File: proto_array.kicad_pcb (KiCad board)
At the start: 2 copper layers, 99.1 x 129.5 mm, 55 parts, among them P1 CONN_01X03, U1 ADS131E08, U2 BEAGLEBONEBLACK

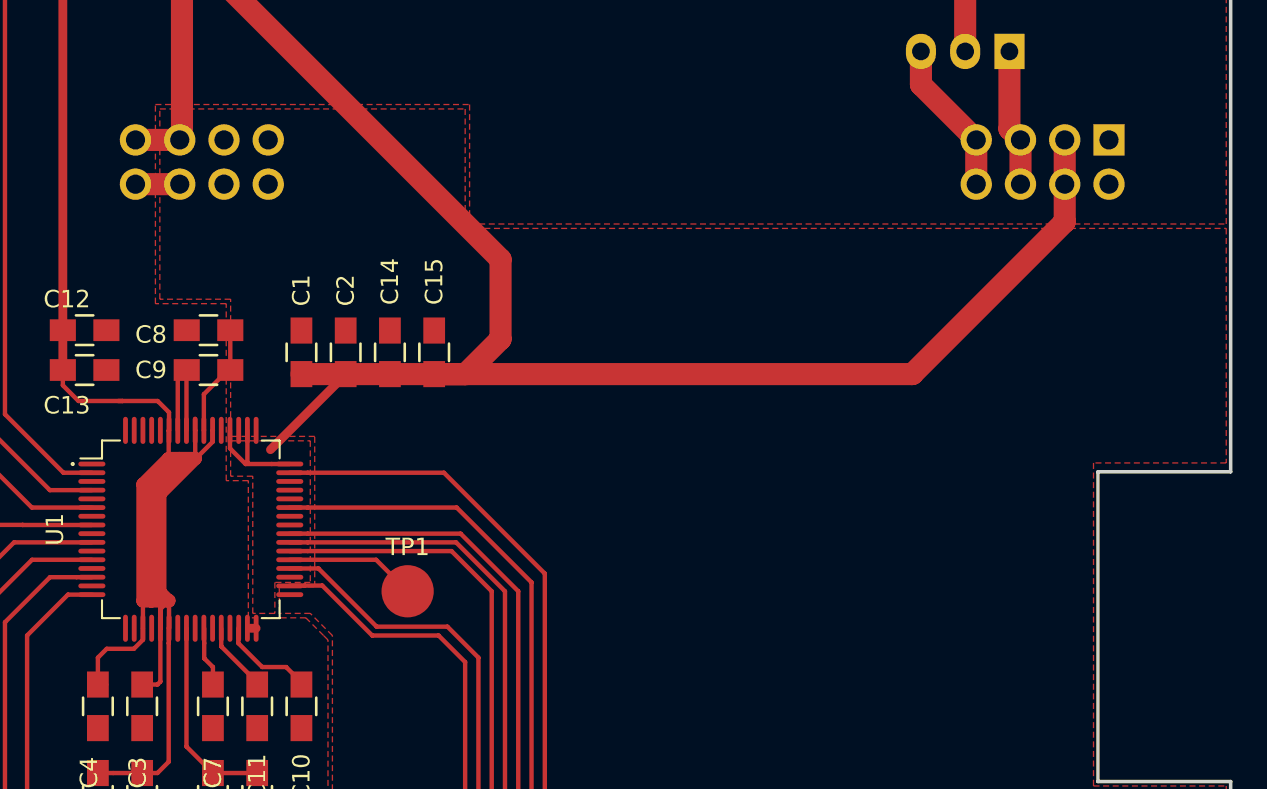
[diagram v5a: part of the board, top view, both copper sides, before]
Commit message: Final board version...
* Fix ADC net DRC (clearance: 8 mils)
* Fix a few track-pad clearance violations
* Fix ground plane pours

Signed-off-by: Chamon <[luizchamon@gmail.com>
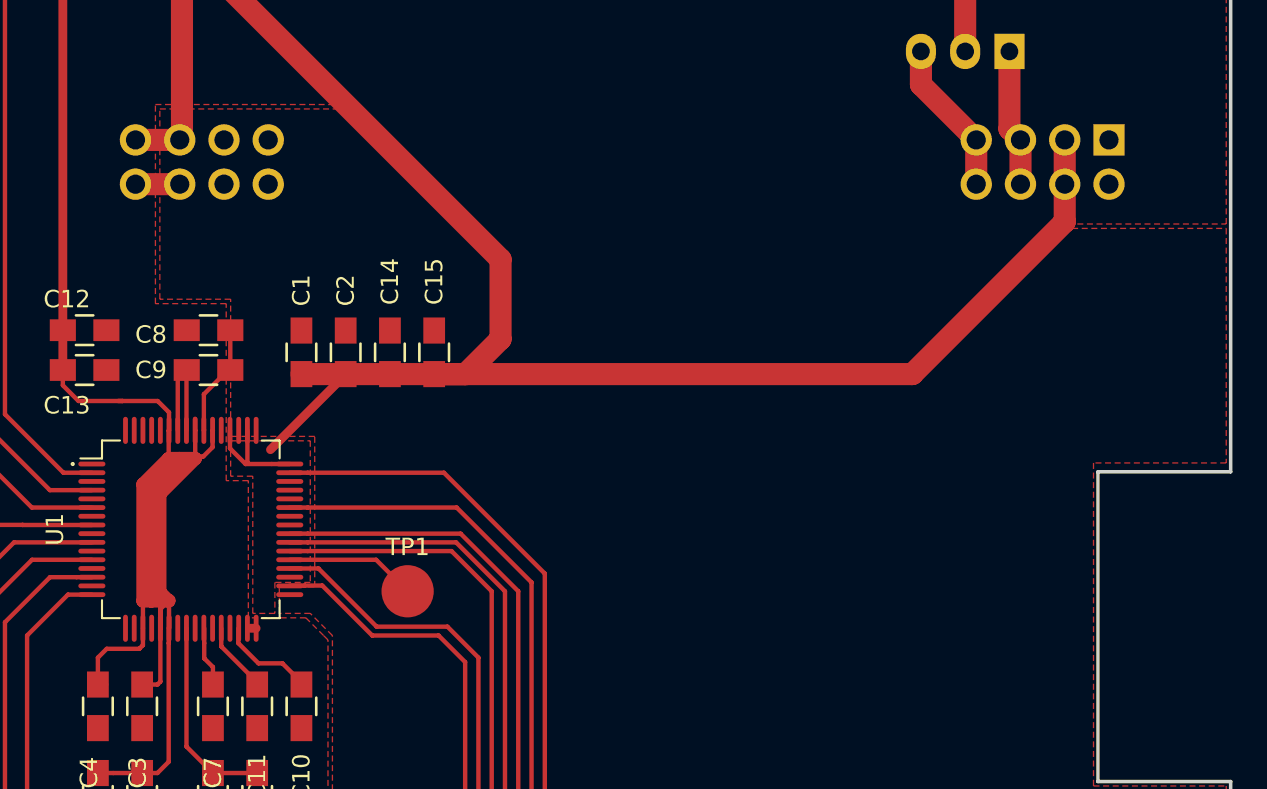
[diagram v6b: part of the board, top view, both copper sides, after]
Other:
- net class ADC: clearance 0.1016 -> 0.2032
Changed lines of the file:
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@@
   (general
     (links 143)
-    (no_connects 57)
+    (no_connects 1)
     (area 9.780001 16.409999 150.304501 157.640001)
     (thickness 1.6)
@@
   )
   (setup
-    (last_trace_width 1.27)
+    (last_trace_width 0.254)
     (user_trace_width 0.2032)
     (user_trace_width 0.254)
@@
   )
   (net_class ADC ""
-    (clearance 0.1016)
+    (clearance 0.2032)
     (trace_width 0.254)
     (via_dia 0.6)
@@
   (segment (start 79.611 69.088) (end 79.736 69.088) (width 0.254) (layer F.Cu) (net 3))
   (segment (start 78.232 72.53986) (end 78.2193 72.55256) (width 0.254) (layer F.Cu) (net 3))
+  (segment (start 83.82 87.142) (end 83.82 87.017) (width 0.254) (layer F.Cu) (net 4))
+  (segment (start 83.82 87.017) (end 82.72866 85.92566) (width 0.254) (layer F.Cu) (net 4))
+  (segment (start 82.72866 85.92566) (end 81.356405 85.92566) (width 0.254) (layer F.Cu) (net 4))
+  (segment (start 81.356405 85.92566) (end 80.19795 84.767205) (width 0.254) (layer F.Cu) (net 4))
   (segment (start 80.19795 84.767205) (end 80.19795 83.91144) (width 0.254) (layer F.Cu) (net 4))
-  (segment (start 81.568745 86.138) (end 80.19795 84.767205) (width 0.254) (layer F.Cu) (net 4))
-  (segment (start 82.941 86.138) (end 81.568745 86.138) (width 0.254) (layer F.Cu) (net 4))
-  (segment (start 83.82 87.017) (end 82.941 86.138) (width 0.254) (layer F.Cu) (net 4))
-  (segment (start 83.82 87.142) (end 83.82 87.017) (width 0.254) (layer F.Cu) (net 4))
   (segment (start 79.21752 84.94522) (end 79.21752 83.91144) (width 0.254) (layer F.Cu) (net 5))
   (segment (start 79.21752 84.95452) (end 79.21752 84.94522) (width 0.254) (layer F.Cu) (net 5))
@@
   (segment (start 78.74 92.222) (end 81.28 92.222) (width 0.254) (layer F.Cu) (net 6))
   (segment (start 77.22108 90.70308) (end 78.74 92.222) (width 0.254) (layer F.Cu) (net 6))
+  (segment (start 74.72172 83.91144) (end 74.72172 84.88172) (width 0.254) (layer F.Cu) (net 7))
+  (segment (start 74.72172 84.88172) (end 74.51344 85.09) (width 0.254) (layer F.Cu) (net 7))
+  (segment (start 74.51344 85.09) (end 72.644 85.09) (width 0.254) (layer F.Cu) (net 7))
+  (segment (start 72.644 85.09) (end 72.136 85.598) (width 0.254) (layer F.Cu) (net 7))
+  (segment (start 72.136 85.598) (end 72.136 87.142) (width 0.254) (layer F.Cu) (net 7))
+  (segment (start 78.71968 72.55256) (end 78.71968 73.51776) (width 0.254) (layer F.Cu) (net 7))
+  (segment (start 78.71968 73.51776) (end 78.18735 74.05009) (width 0.254) (layer F.Cu) (net 7))
+  (segment (start 78.18735 74.05009) (end 77.724 74.05009) (width 0.254) (layer F.Cu) (net 7))
   (segment (start 70.124 66.802) (end 70.124 69.088) (width 0.508) (layer F.Cu) (net 7))
   (segment (start 77.724 74.168) (end 77.724 74.05009) (width 0.254) (layer F.Cu) (net 7))
   (segment (start 77.724 74.05009) (end 77.724 72.55764) (width 0.254) (layer F.Cu) (net 7))
-  (segment (start 78.71968 72.55256) (end 78.71968 73.213128) (width 0.254) (layer F.Cu) (net 7))
-  (segment (start 78.71968 73.213128) (end 77.882718 74.05009) (width 0.254) (layer F.Cu) (net 7))
-  (segment (start 77.882718 74.05009) (end 77.724 74.05009) (width 0.254) (layer F.Cu) (net 7))
   (segment (start 75.204452 82.34172) (end 76.19492 82.34172) (width 0.762) (layer F.Cu) (net 7))
   (segment (start 74.72172 82.34172) (end 75.204452 82.34172) (width 0.762) (layer F.Cu) (net 7))
@@
   (segment (start 74.72172 83.91144) (end 74.72172 82.34172) (width 0.254) (layer F.Cu) (net 7))
   (segment (start 76.19999 84.767205) (end 76.19999 83.91144) (width 0.254) (layer F.Cu) (net 7))
-  (segment (start 72.644 85.09) (end 72.136 85.598) (width 0.254) (layer F.Cu) (net 7))
-  (segment (start 72.136 85.598) (end 72.136 87.142) (width 0.254) (layer F.Cu) (net 7))
   (segment (start 72.136 87.017) (end 72.136 87.142) (width 0.254) (layer F.Cu) (net 7))
   (segment (start 74.168 92.222) (end 74.168 92.097) (width 0.254) (layer F.Cu) (net 7))
@@
   (segment (start 56.669411 19.05) (end 53.34 19.05) (width 1.27) (layer F.Cu) (net 7))
   (segment (start 78.071558 19.05) (end 56.669411 19.05) (width 1.27) (layer F.Cu) (net 7))
-  (segment (start 74.203728 85.09) (end 72.644 85.09) (width 0.254) (layer F.Cu) (net 7))
-  (segment (start 74.72172 84.572008) (end 74.203728 85.09) (width 0.254) (layer F.Cu) (net 7))
-  (segment (start 74.72172 83.91144) (end 74.72172 84.572008) (width 0.254) (layer F.Cu) (net 7))
   (segment (start 75.72248 86.97452) (end 75.555 87.142) (width 0.254) (layer F.Cu) (net 7))
   (segment (start 75.555 87.142) (end 74.676 87.142) (width 0.254) (layer F.Cu) (net 7))
@@
         (xy 38.354 145.796) (xy 71.12 145.796) (xy 71.12 96.266) (xy 85.344 96.266) (xy 85.344 84.582)
         (xy 85.09 84.328) (xy 84.074 83.312) (xy 80.772 83.312) (xy 80.772 75.438) (xy 79.502 75.438)
-        (xy 79.502 65.278) (xy 75.438 65.278) (xy 75.438 53.848) (xy 93.472 53.848) (xy 93.472 60.706)
-        (xy 136.906 60.706) (xy 136.906 16.764) (xy 79.502 16.764) (xy 38.354 16.764)
+        (xy 79.502 65.278) (xy 75.438 65.278) (xy 75.438 53.848) (xy 86.614 53.848) (xy 95.504 62.738)
+        (xy 95.504 67.31) (xy 93.726 69.088) (xy 118.872 69.088) (xy 127.254 60.706) (xy 136.906 60.706)
+        (xy 136.906 16.764) (xy 79.502 16.764) (xy 38.354 16.764)
       )
     )
@@
       (pts
         (xy 84.582 72.898) (xy 79.756 72.898) (xy 79.756 65.024) (xy 75.692 65.024) (xy 75.692 54.102)
-        (xy 93.218 54.102) (xy 93.218 60.96) (xy 131.826 60.96) (xy 131.826 60.96) (xy 136.906 60.96)
-        (xy 136.906 74.422) (xy 129.286 74.422) (xy 129.286 92.964) (xy 136.906 92.964) (xy 136.906 145.796)
-        (xy 71.374 145.796) (xy 71.374 96.52) (xy 85.598 96.52) (xy 85.598 84.328) (xy 84.328 83.058)
-        (xy 82.55 83.058) (xy 82.55 81.534) (xy 84.582 81.534)
+        (xy 86.36 54.102) (xy 93.218 60.96) (xy 95.25 62.992) (xy 95.25 67.31) (xy 93.218 69.342)
+        (xy 119.126 69.342) (xy 127.508 60.96) (xy 136.906 60.96) (xy 136.906 74.422) (xy 129.286 74.422)
+        (xy 129.286 92.964) (xy 136.906 92.964) (xy 136.906 145.796) (xy 71.374 145.796) (xy 71.374 96.52)
+        (xy 85.598 96.52) (xy 85.598 84.328) (xy 84.328 83.058) (xy 82.55 83.058) (xy 82.55 81.534)
+        (xy 84.582 81.534)
       )
     )

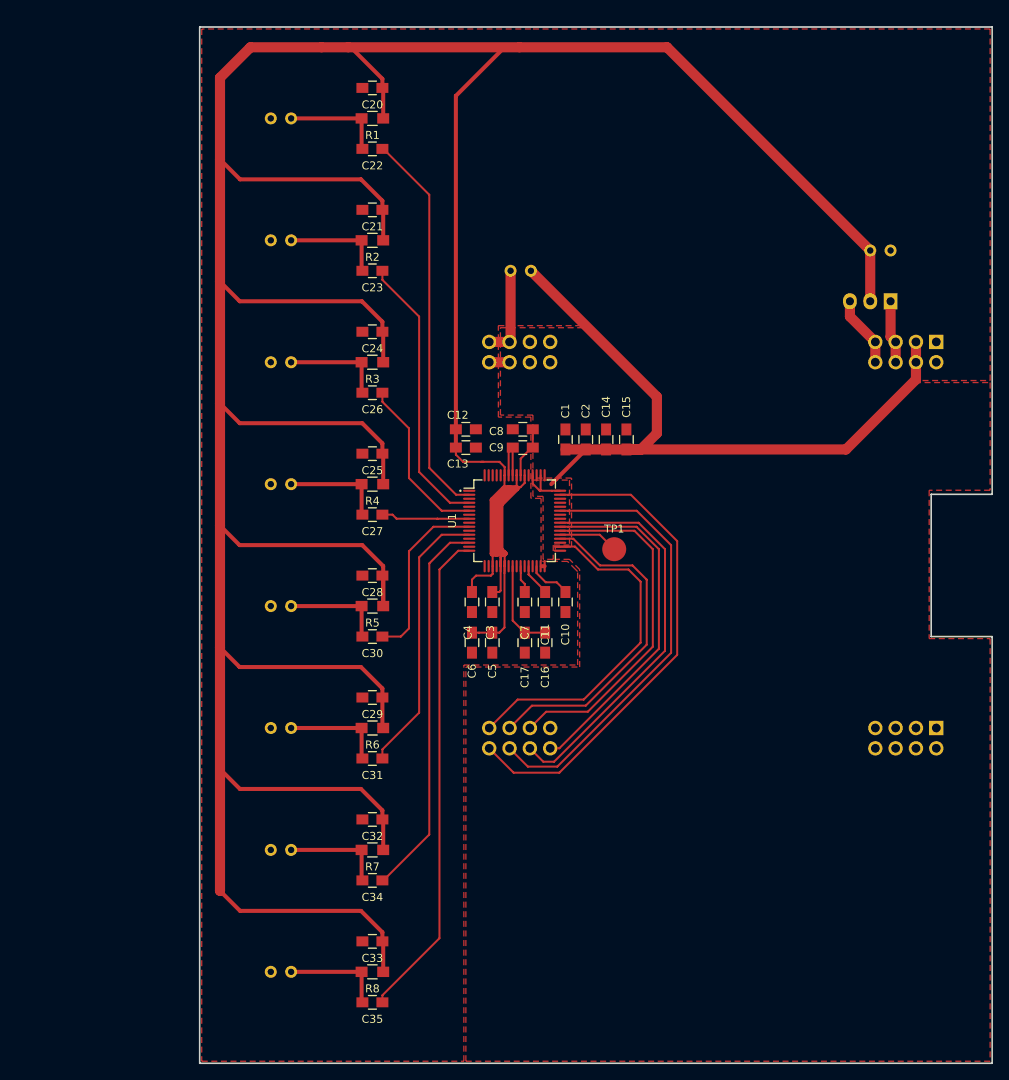
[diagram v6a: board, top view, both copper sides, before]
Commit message: Unify drill sizes (all drilling in 0.8 mm).
Signed-off-by: Chamon <[luizchamon@gmail.com>
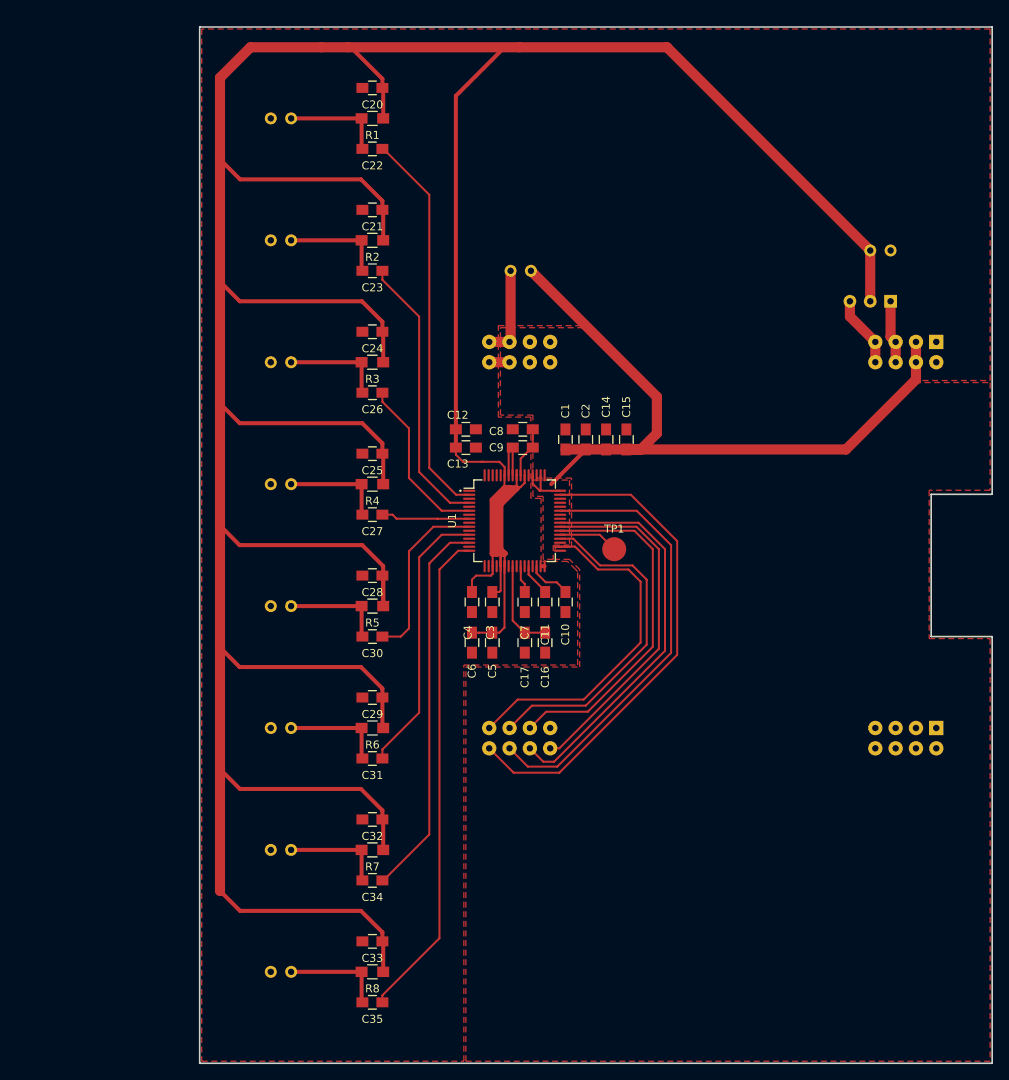
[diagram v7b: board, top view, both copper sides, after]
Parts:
- MIC1, MIC2, MIC3, MIC4, MIC5, MIC6, MIC7, MIC8: footprint Capacitors_Elko_ThroughHole:Elko_vert_20x10mm_RM2.5_CopperClear -> micarray:Electret_1mm
- P1: footprint Pin_Headers:Pin_Header_Straight_1x03 -> micarray:Pin_Header_01x03
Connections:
- net /SPI0_CLK renamed Net-(U2-PadC22)
- net /SPI0_CS renamed Net-(U2-PadC17)
- net /SPI0_MISO renamed Net-(U2-PadC21)
- net /SPI0_MOSI renamed Net-(U2-PadC18)

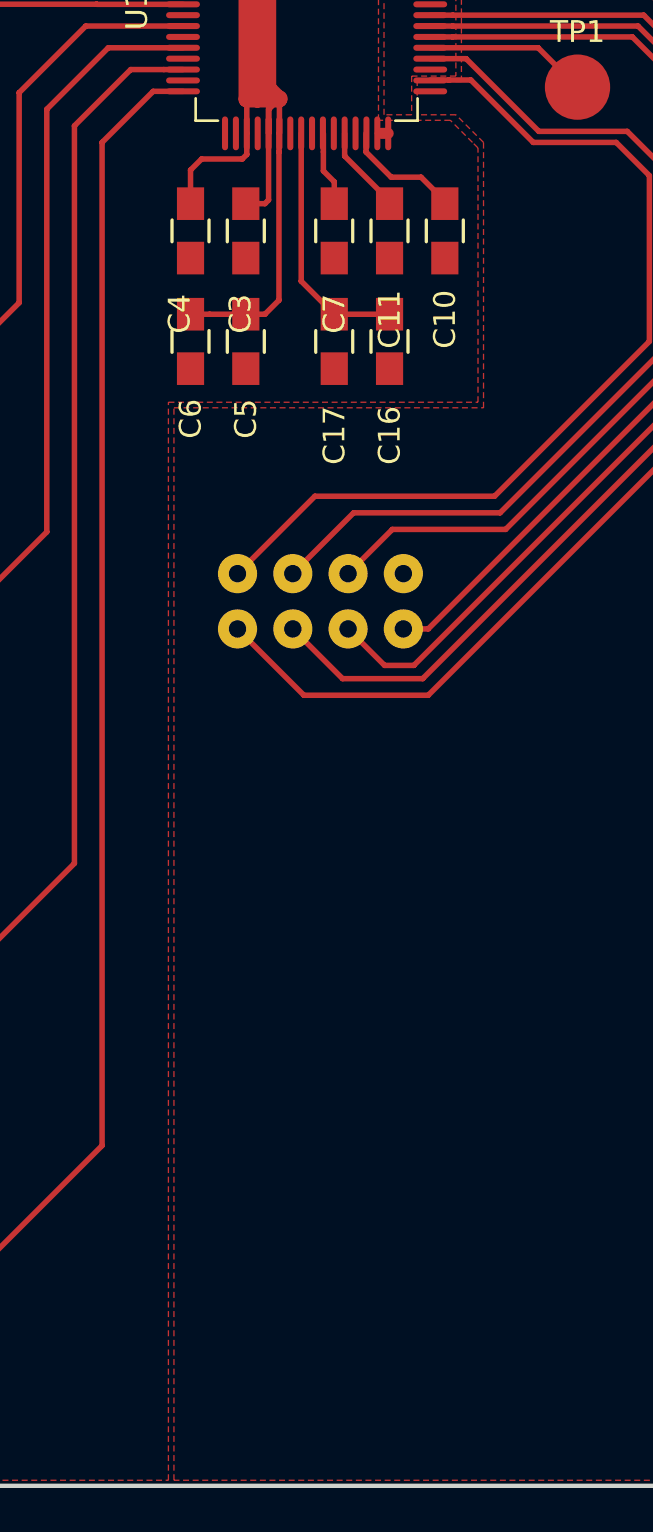
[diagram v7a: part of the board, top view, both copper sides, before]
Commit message: Update tantalum capacitor (C11) package.
Signed-off-by: Chamon <luizchamon@gmail.com>
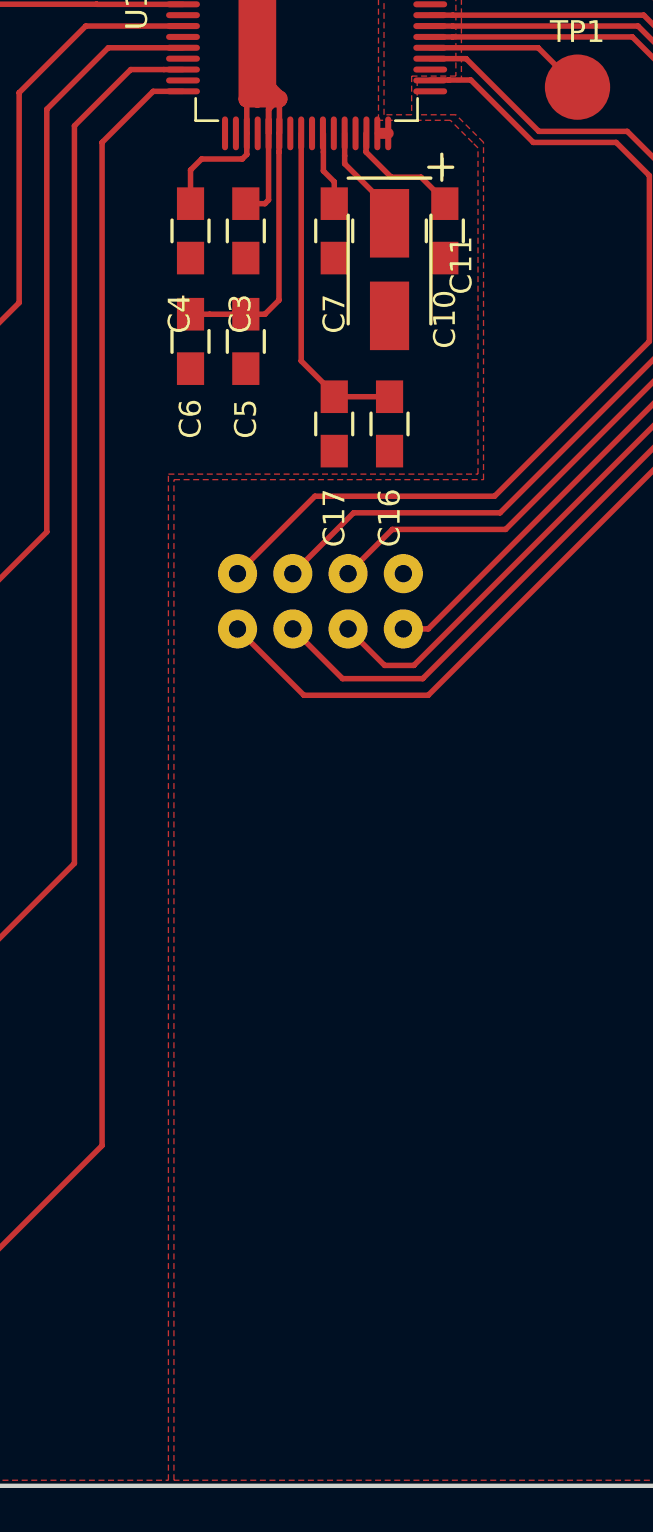
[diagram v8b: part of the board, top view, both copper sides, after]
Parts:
- C11: footprint Capacitors_SMD:C_0805_HandSoldering -> Capacitors_Tantalum_SMD:TantalC_SizeB_EIA-3528_HandSoldering
- moved C16 3.79 mm to (81.3, 97.3)
- moved C17 3.79 mm to (78.7, 97.3)
- moved C11 1.78 mm to (81.3, 90.2)
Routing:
- net /VREFP: track 11.5 -> 15.4 mm
- net Net-(C11-Pad1): track 4.08 -> 4.99 mm
